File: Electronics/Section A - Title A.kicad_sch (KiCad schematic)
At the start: 9 parts, among them J1 THD-02-R, J2 HDMI_A, J3 Conn_01x22_Female, U1 RT9742SNGV

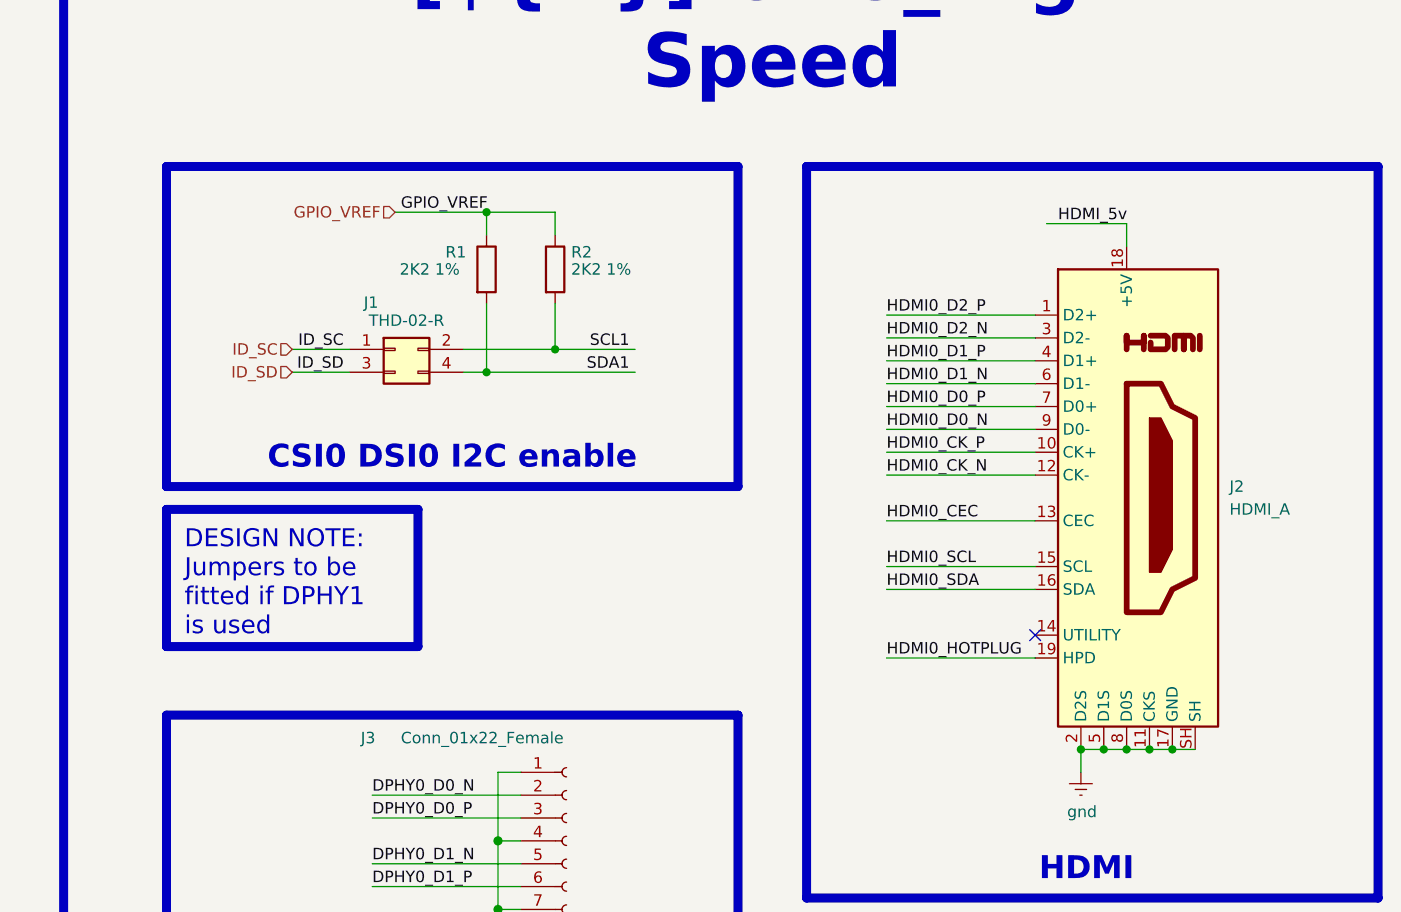
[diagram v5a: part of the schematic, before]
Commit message: Changed sata port
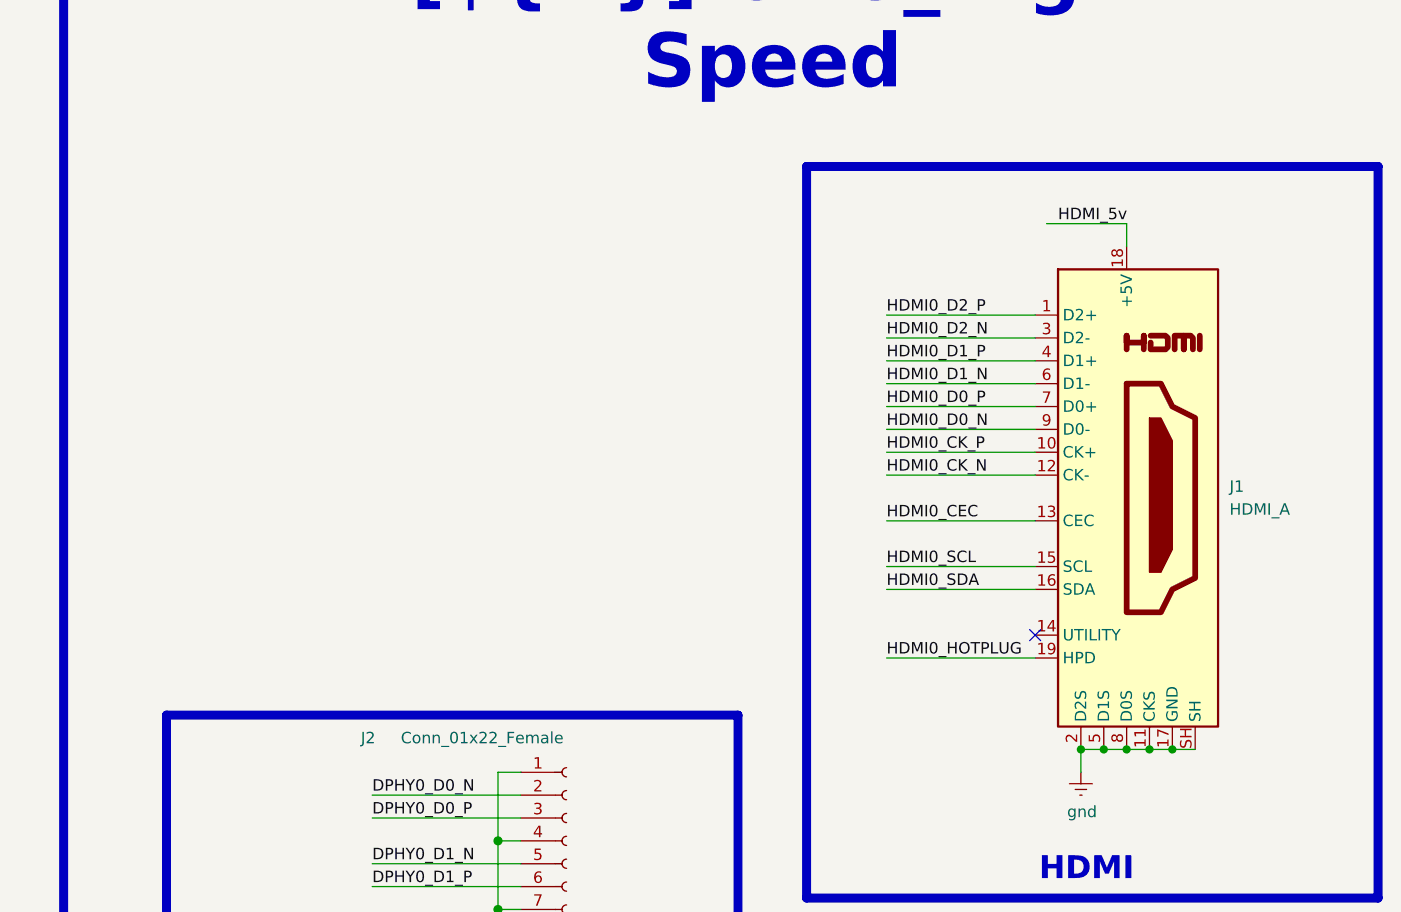
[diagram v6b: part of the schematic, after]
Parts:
- removed J1: THD-02-R, Connector_PinHeader_2.54mm:PinHeader_2x02_P2.54mm_Vertical, symbol Connector_Generic:Conn_02x02_Odd_Even
- removed R1, R2: 2K2 1%, Resistor_SMD:R_0603_1608Metric, symbol Device:R
- renumbered J2 to J1, J3 to J2

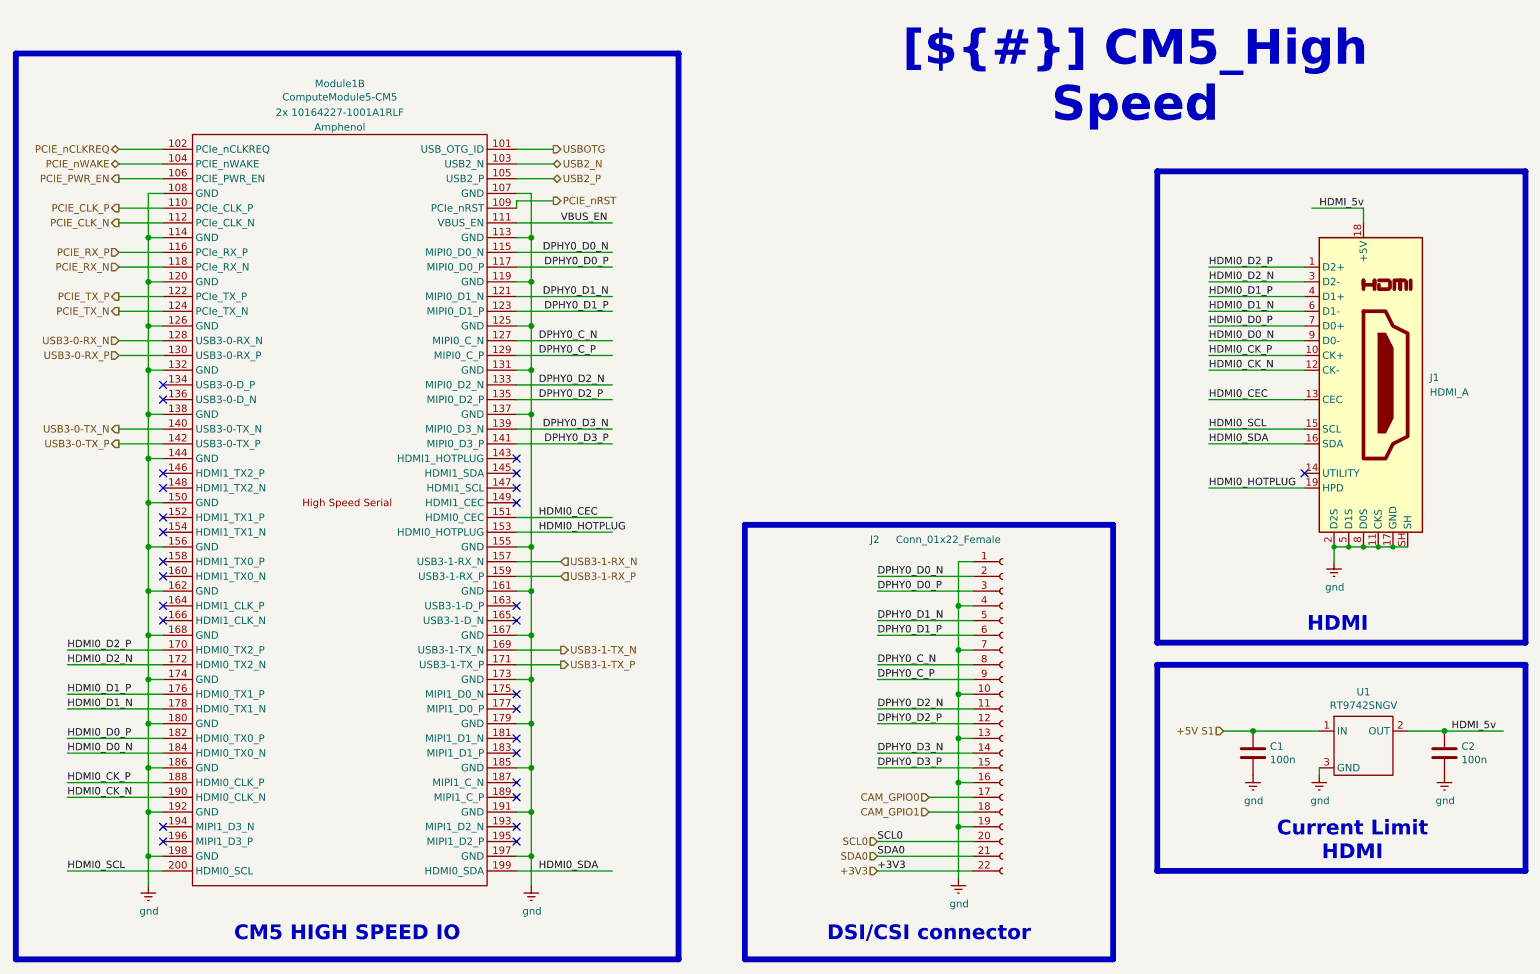
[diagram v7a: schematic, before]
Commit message: More pcb arangment, verticle ports
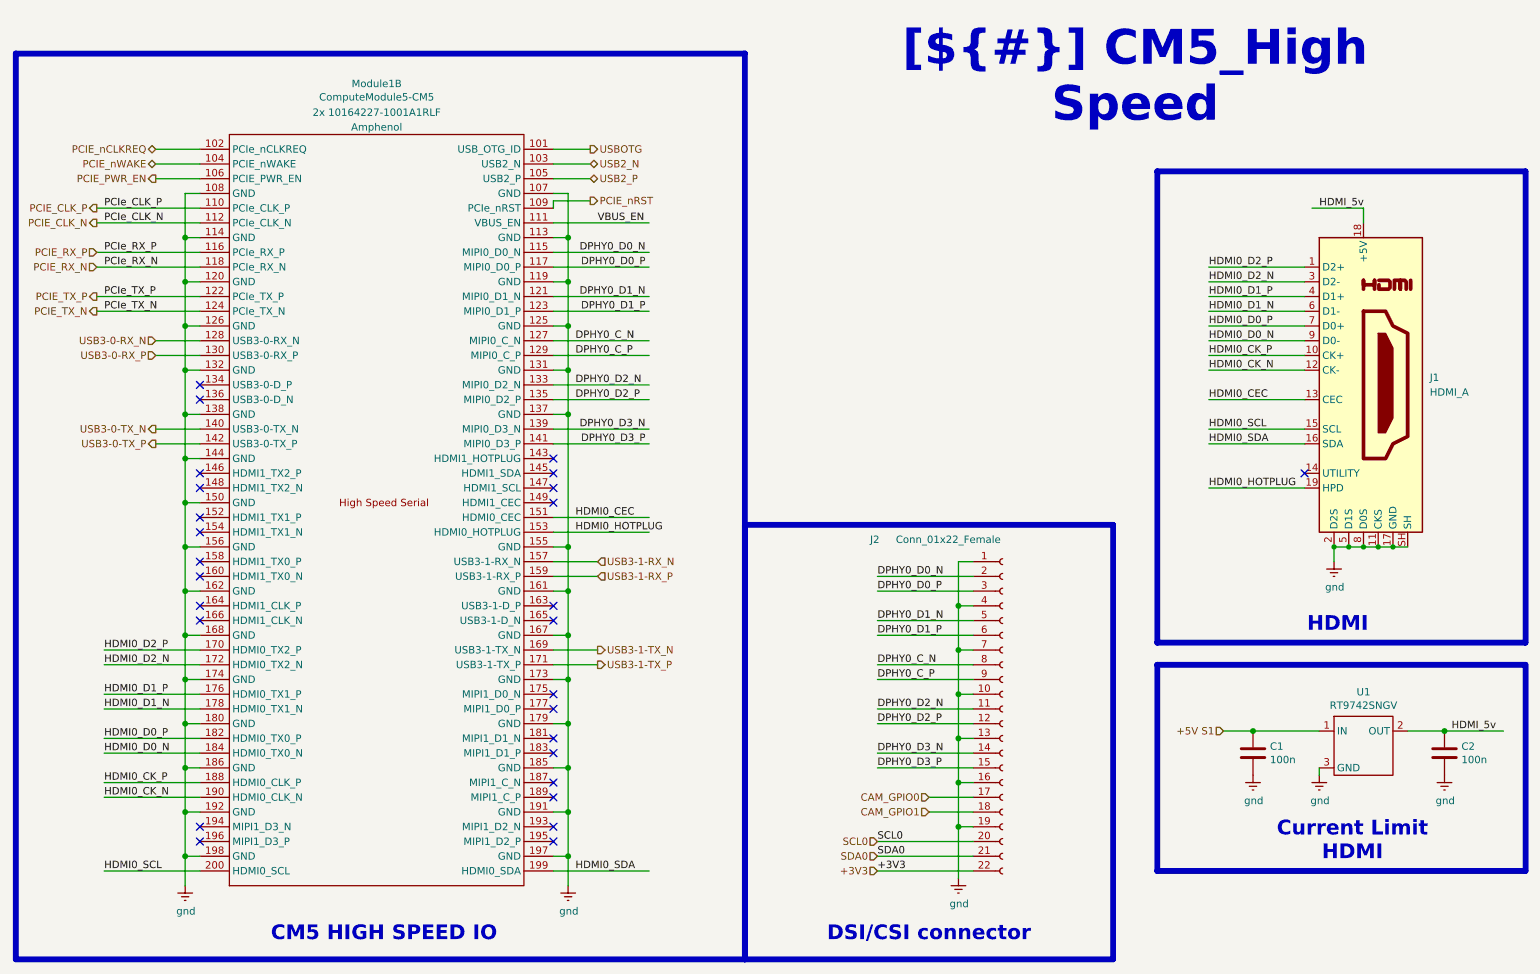
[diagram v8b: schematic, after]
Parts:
- J1: footprint 10029449-111RLF:AMPHENOL_10029449-111RLF -> G45A19071083HR:AMPHENOL_G45A19071083HR
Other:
- moved on the sheet: Module1B
